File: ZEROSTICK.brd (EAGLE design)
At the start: 78 x 34 mm, 47 parts, among them IC1 ATMEGA32U4NT-TQFP, IC2 HX711-SOP16L, J1 RJ10-WURTH, J2 AUDIO-JACK-PJ321, J3 USB-C-16P-16P, K1 HE721C-DIP, Q1 2N7002, Q2 2N3906, SW1 SWITCH-SPDT-4TABSSMT, SW2 SWITCH-SPDT-4TABSSMT, SW3 RESET, SW4 Trigger Level, SW5 Tare

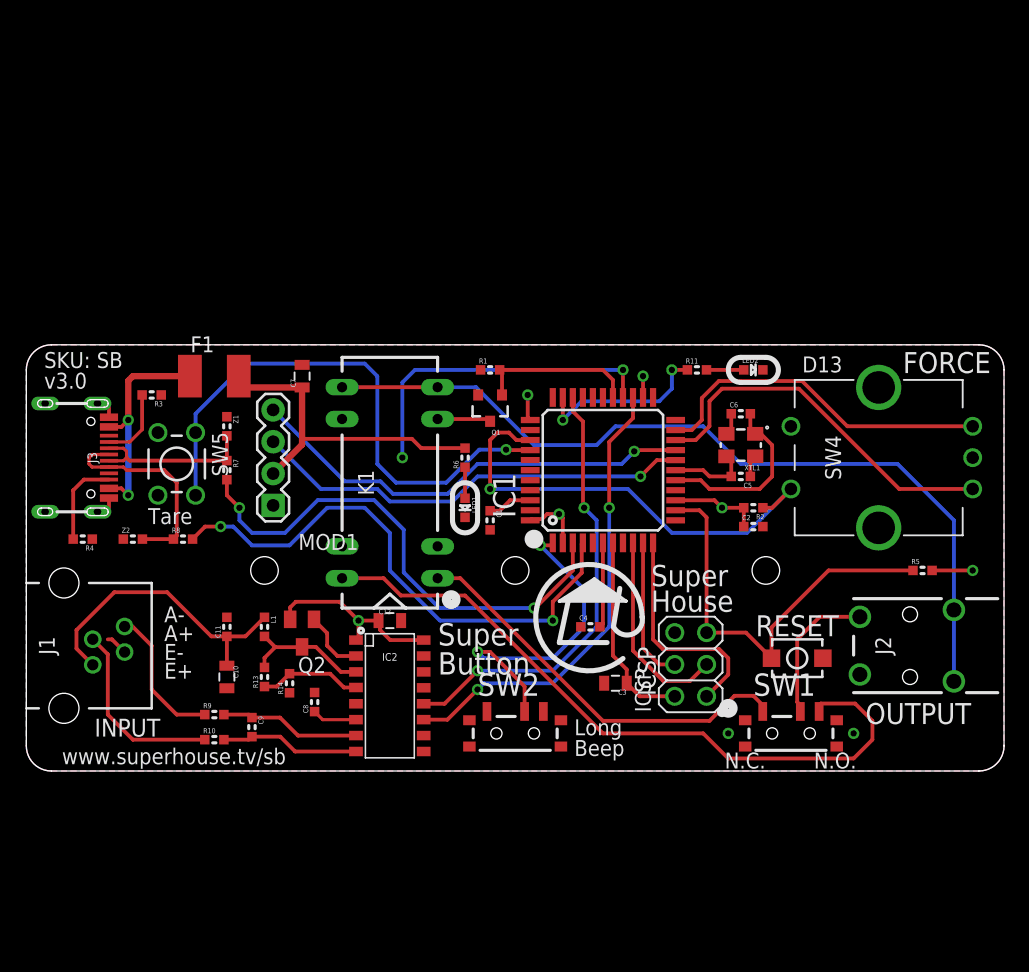
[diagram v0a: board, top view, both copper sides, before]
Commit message: Partical conversion from SB project
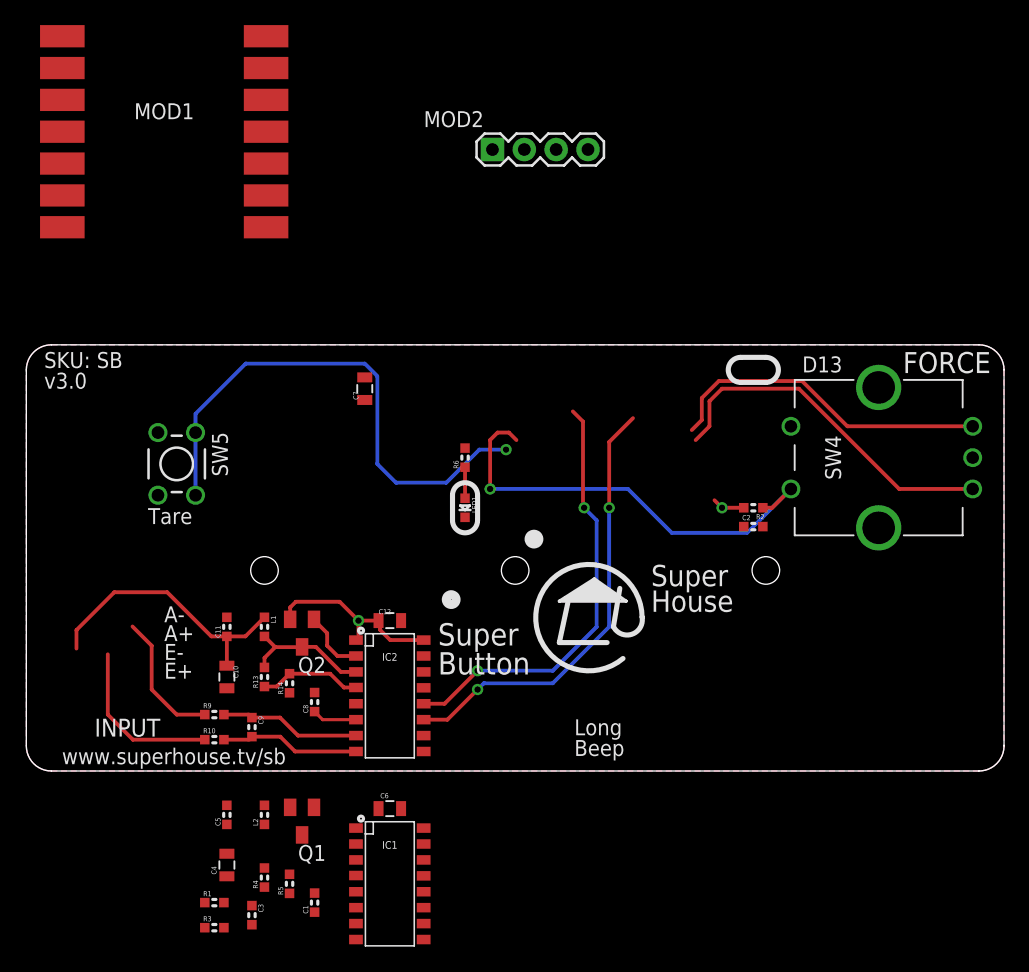
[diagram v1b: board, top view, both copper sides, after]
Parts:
- removed F1: 500mA PTC 1812, SuperHouse-Fuses:1812
- removed ICSP: ICSP, SuperHouse-Connectors:2X03-ICSP
- removed J1: RJ10-WURTH, SuperHouse-Connectors:RJ10
- removed J2: AUDIO-JACK-PJ321, SuperHouse-Connectors:AUDIO-JACK-PJ321
- removed J3: USB-C-16P-16P, SuperHouse-Connectors:USB-C-16P
- removed K1: HE721C-DIP, SuperHouse-Relays:HE721
- removed LED2: GREEN, SuperHouse-LEDs:LED-0603
- removed R11: 1K, SuperHouse-DiscreteSemi:R0603
- removed R7, R8: 22R, SuperHouse-DiscreteSemi:R0603
- removed SW1, SW2: SWITCH-SPDT-4TABSSMT, SuperHouse-Switches:MK-12C02
- removed SW3: RESET, SuperHouse-Switches:TACTILE_SMT_3X4X2
- removed XTL1: 16MHz, SuperHouse-Oscillators:CRYSTAL-SMD-3X2
- removed Z1, Z2: PGB1010603, SuperHouse-DiscreteSemi:TVS0603
- added L2: 3.3uH, SuperHouse-DiscreteSemi:L0603
- added MOD2: OLED-I2C-128X64-0.96-HEADER, SuperHouse-Displays:OLED-128X64-0.96-HEADER
- C3: value 10uF -> 100nF; device SuperHouse-DiscreteSemi:C0805 -> SuperHouse-DiscreteSemi:C0603
- C4: value 1uF -> 10uF; device SuperHouse-DiscreteSemi:C0603 -> SuperHouse-DiscreteSemi:C0805
- C5: value 15pF -> 100nF
- C6: value 15pF -> 10uF; device SuperHouse-DiscreteSemi:C0603 -> SuperHouse-DiscreteSemi:C0805
- IC1: value ATMEGA32U4NT-TQFP -> HX711-SOP16L; device SuperHouse-MCUs:TQFP44 -> SuperHouse-ICs:SOP16-L
- MOD1: value OLED-I2C-128X32-0.91-HEADER -> XIAO-SMT; device SuperHouse-Displays:OLED-128X32-0.91-HEADER -> SuperHouse-Modules:XIAO-SMT
- Q1: value 2N7002 -> 2N3906; device SuperHouse-DiscreteSemi:SOT23-3 -> SuperHouse-DiscreteSemi:SOT23-BEC
- R1: value 10K -> 100R
- R3: value 5k1 -> 100R
- R4: value 5k1 -> 10K
- R5: value 10K -> 8K2
- SW4: value Trigger Level -> Sensitivity
- moved R5 56.3 mm to (21.0, -9.00), turned to 90 degrees
- moved C5 49.1 mm to (16.0, -3.50), turned to 90 degrees
- moved R1 47.9 mm to (15.0, -10.5)
- moved R3 42.8 mm to (15.0, -12.5), turned to 0 degrees
- moved C6 42.1 mm to (29.0, -3.00)
- moved MOD1 37.5 mm to (11.0, 51.0)
- moved IC1 37.1 mm to (29.0, -9.00), turned to 0 degrees
- moved Q1 36.2 mm to (22.0, -4.00)
- moved C4 34.7 mm to (16.0, -7.50), turned to 90 degrees
- moved C3 34.4 mm to (18.0, -11.5), turned to 270 degrees
- moved C1 33.6 mm to (23.0, -10.5), turned to 90 degrees
- moved R4 30.6 mm to (19.0, -8.50), turned to 90 degrees
- moved C7 5.10 mm to (27.0, 30.5)
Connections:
- removed net 3V3: C4.2, IC1.6
- removed net A+: J1.P$3, R10.1
- removed net A-: J1.P$4, R9.1
- removed net A0: IC1.36, R2.1, SW4.SW1
- removed net A1: IC1.37, SW5.1, SW5.2
- removed net A2: IC1.38
- removed net A3: IC1.39
- removed net A4: IC1.40
- removed net A5: IC1.41
- removed net AREF: C1.1, IC1.42
- removed net D+: J3.A6, J3.B6, R8.1, Z2.2
- removed net D-: J3.A7, J3.B7, R7.1, Z1.2
- removed net D10_A11: IC1.30
- removed net D11: IC1.12
- removed net D12: IC1.26
- removed net D13: IC1.32, R11.1
- removed net D2_SDA: IC1.19, MOD1.SDA
- removed net D3_SCL: IC1.18, MOD1.SCL
- removed net D4_A6: IC1.25, IC2.11
- removed net D5: IC1.31, IC2.12
- removed net D6_A8: IC1.27, Q1.1, R1.2
- removed net D7_AIN0: IC1.1, SW2.2
- removed net D8_A9: IC1.28
- removed net D9_A10: IC1.29
- removed net E+: C10.1, C11.1, J1.P$1, L1.1
- removed net HWB: IC1.33
- removed net MISO: IC1.11, ICSP.1
- removed net MOSI: IC1.10, ICSP.4
- removed net N$10: J3.B5, R4.2
- removed net N$11: C5.2, IC1.17, XTL1.3
- removed net N$12: C6.2, IC1.16, XTL1.1
- removed net N$13: J3.A5, R3.2
- removed net N$9: J2.3, SW1.2
- removed net RD+: IC1.4, R8.2
- removed net RD-: IC1.3, R7.2
- removed net RESET: IC1.13, ICSP.5, R5.1, SW3.2
- removed net RXLED_SS: IC1.8
- removed net SCK: IC1.9, ICSP.3
- removed net TX_LED: IC1.22
- removed net USB+: F1.1, J3.A4B9, J3.A9B4
- new net 3.3V: C12.1, C2.1, C6.1, C7.1, IC1.1, IC1.16, IC2.1, IC2.16, MOD1.12, MOD2.VCC, Q1.E, Q2.E, R2.2, R6.2
- new net D10_MOSI: MOD1.11
- new net D2: IC1.12, MOD1.3
- new net D3: IC1.11, MOD1.4
- new net D4_SDA: MOD1.5, MOD2.SDA
- new net D5_SCL: MOD1.6, MOD2.SCL
- new net D6_TX: MOD1.7, SW5.1, SW5.2
- new net D7_RX: MOD1.8, R2.1, SW4.SW1
- new net D8_SCK: MOD1.9, SW4.A
- new net D9_MISO: MOD1.10, SW4.B
- new net N$2: C3.2, IC1.8, R3.2
- new net X_A+: R10.1
- new net X_A-: R9.1
- new net X_E+: C10.1, C11.1, L1.1
- new net Y_A+: R3.1
- new net Y_A-: R1.1
- new net Y_E+: C4.1, C5.1, L2.1
- net 5V: now also MOD1.14; no longer C12.1, C2.1, C3.1, C7.1, F1.2, IC1.14, IC1.2, IC1.24, IC1.34, IC1.44, IC1.7, IC2.1, IC2.16, ICSP.2, K1.2, MOD1.VCC, Q2.E, R2.2, R5.2, R6.2
- net D0: now also IC2.12, MOD1.1; no longer IC1.20, SW4.A
- net D1: now also IC2.11, MOD1.2; no longer IC1.21, SW4.B
- net GND: now also C4.2, C5.2, C6.2, IC1.14, MOD1.13, MOD2.GND, R5.1; no longer C3.2, C4.1, C5.1, C6.1, IC1.23, IC1.35, IC1.43, ICSP.6, J1.P$2, J3.A12B1, J3.A1B12, J3.FIX1, J3.FIX2, J3.FIX3, J3.FIX4, LED2.C, MOD1.GND, Q1.2, R1.1, R3.1, R4.1, SW1.MNT@1, SW1.MNT@2, SW1.MNT@3, SW1.MNT@4, SW2.3, SW2.MNT@1, SW2.MNT@2, SW2.MNT@3, SW2.MNT@4, SW3.1, XTL1.2, XTL1.4, Z1.1, Z2.1
- net N$1: now also C3.1, IC1.7, R1.2; no longer LED2.A, R11.2
- net N$3: now also C1.1, IC1.6; no longer K1.6, Q1.3
- net N$4: now also IC1.2, Q1.B; no longer K1.14, SW1.3
- net N$6: now also IC1.4, R4.1, R5.2; no longer K1.1, SW1.1
- net N$7: now also IC1.3, L2.2, Q1.C, R4.2; no longer J2.4A, J2.4B, K1.7, K1.8
- net XO: now also IC1.13
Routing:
- net 5V: track 78.0 -> 0.00 mm, vias 6 -> 0
- net N$7: track 67.3 -> 0.00 mm
- net N$4: track 55.8 -> 0.00 mm
- net A1: track 44.0 -> 0.00 mm, vias 1 -> 0
- net RD+: track 43.7 -> 0.00 mm, vias 2 -> 0
- net D6_TX: track 0.00 -> 42.1 mm, vias 0 -> 1
- net RD-: track 40.8 -> 0.00 mm, vias 2 -> 0
- net A0: track 37.4 -> 0.00 mm, vias 1 -> 0
- net D4_A6: track 37.0 -> 0.00 mm, vias 2 -> 0
- net D2_SDA: track 36.3 -> 0.00 mm, vias 1 -> 0
- net D7_RX: track 0.00 -> 36.3 mm, vias 0 -> 1
- net D3_SCL: track 35.5 -> 0.00 mm, vias 1 -> 0
- net D5: track 35.4 -> 0.00 mm, vias 2 -> 0
- net RESET: track 33.5 -> 0.00 mm
- net N$6: track 32.3 -> 0.00 mm
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- added copper zone on layer 16, net 3.3V
- removed copper zone on layer 16, net 5V
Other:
- board text removed: "ICSP"
- board text removed: "N.C."
- board text removed: "N.O."
- board text removed: "OUTPUT"
- board text removed: "RESET"
